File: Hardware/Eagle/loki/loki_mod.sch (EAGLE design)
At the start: 36 parts

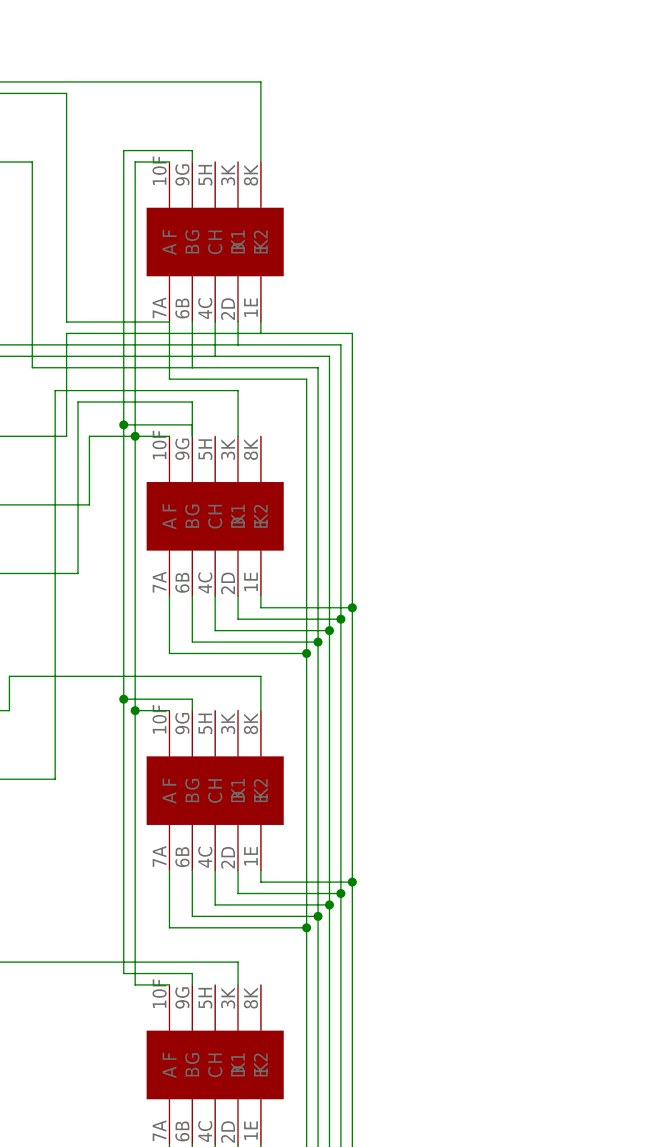
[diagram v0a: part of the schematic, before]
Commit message: Update the watch application to support the Loki module.
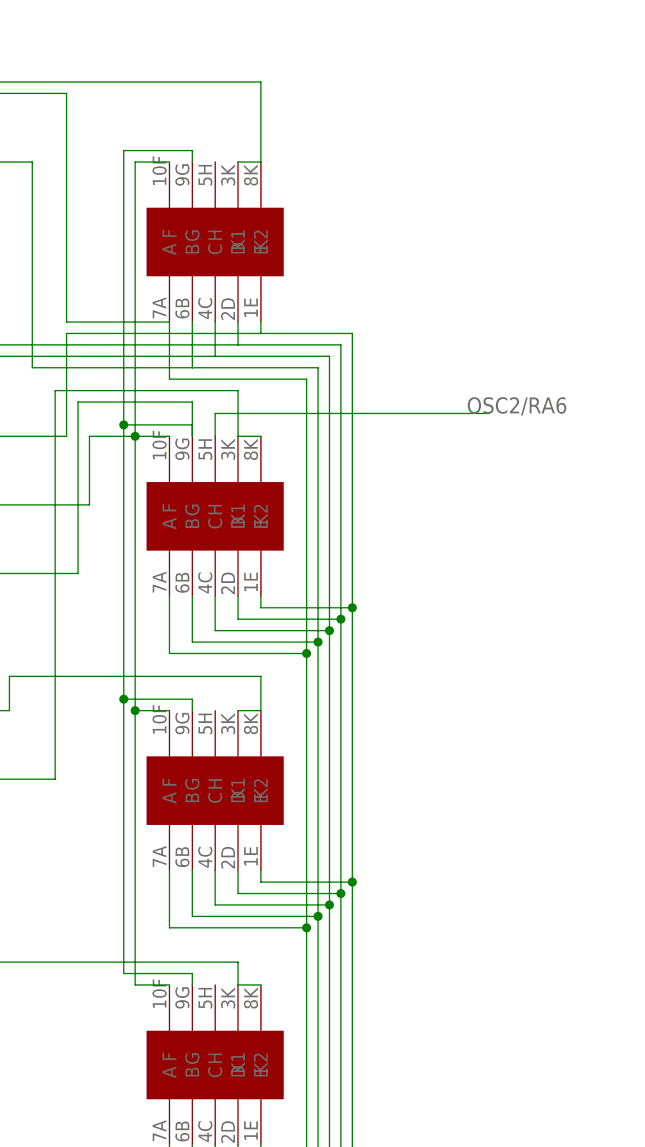
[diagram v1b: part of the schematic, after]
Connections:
- net OSC2/RA6: now also 1H.H
- net PGC/LED_M7: now also 10H.K1
- net RB1/LED_M6: now also 1H.K2
- net RB4/LED_H4: now also 10M.K1
- net RC3/LED_M4: now also 1M.K2
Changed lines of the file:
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@@
 <setting verticaltext="up"/>
 </settings>
-<grid distance="0.05" unitdist="inch" unit="inch" style="lines" multiple="1" display="no" altdistance="0.01" altunitdist="inch" altunit="inch"/>
+<grid distance="0.1" unitdist="inch" unit="inch" style="lines" multiple="1" display="no" altdistance="0.01" altunitdist="inch" altunit="inch"/>
 <layers>
 <layer number="1" name="Top" color="4" fill="1" visible="no" active="no"/>
@@
 <wire x1="-20.32" y1="-41.91" x2="7.62" y2="-41.91" width="0.1524" layer="91"/>
 <wire x1="7.62" y1="-41.91" x2="7.62" y2="-45.72" width="0.1524" layer="91"/>
+<pinref part="10M" gate="G$1" pin="K1"/>
+<wire x1="5.08" y1="-45.72" x2="7.62" y2="-45.72" width="0.1524" layer="91"/>
 </segment>
 </net>
@@
 <wire x1="-21.59" y1="-73.66" x2="5.08" y2="-73.66" width="0.1524" layer="91"/>
 <wire x1="5.08" y1="-73.66" x2="5.08" y2="-76.2" width="0.1524" layer="91"/>
+<pinref part="1M" gate="G$1" pin="K2"/>
+<wire x1="5.08" y1="-76.2" x2="7.62" y2="-76.2" width="0.1524" layer="91"/>
 </segment>
 </net>
@@
 <wire x1="-36.83" y1="24.13" x2="7.62" y2="24.13" width="0.1524" layer="91"/>
 <wire x1="7.62" y1="24.13" x2="7.62" y2="15.24" width="0.1524" layer="91"/>
+<pinref part="10H" gate="G$1" pin="K1"/>
+<wire x1="5.08" y1="15.24" x2="7.62" y2="15.24" width="0.1524" layer="91"/>
 </segment>
 <segment>
@@
 <wire x1="-15.24" y1="-10.16" x2="5.08" y2="-10.16" width="0.1524" layer="91"/>
 <wire x1="5.08" y1="-10.16" x2="5.08" y2="-15.24" width="0.1524" layer="91"/>
+<pinref part="1H" gate="G$1" pin="K2"/>
+<wire x1="5.08" y1="-15.24" x2="7.62" y2="-15.24" width="0.1524" layer="91"/>
 </segment>
 </net>
@@
 <label x="30.48" y="111.76" size="1.778" layer="95"/>
 </segment>
-</net>
+<segment>
+<pinref part="1H" gate="G$1" pin="H"/>
+<wire x1="2.54" y1="-15.24" x2="2.54" y2="-12.7" width="0.1524" layer="91"/>
+<wire x1="2.54" y1="-12.7" x2="33.02" y2="-12.7" width="0.1524" layer="91"/>
+<label x="30.48" y="-12.7" size="1.778" layer="95"/>
+</segment>
+</net>

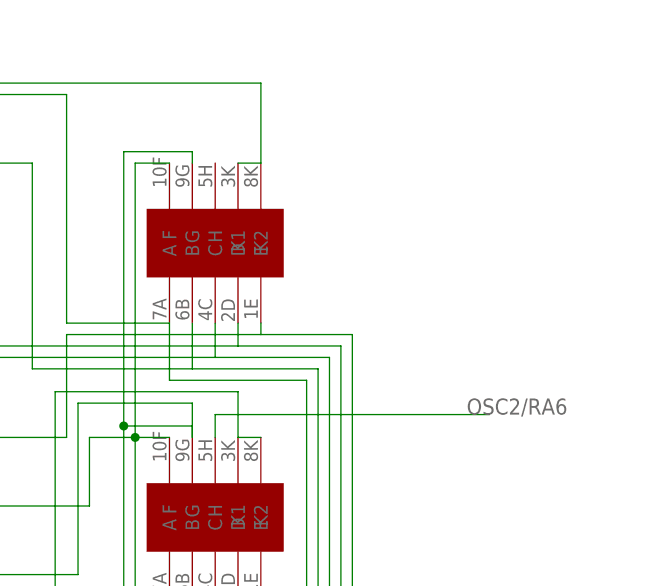
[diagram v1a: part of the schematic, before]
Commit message: Added resitor for date dot, if using the USSR replacement made display.
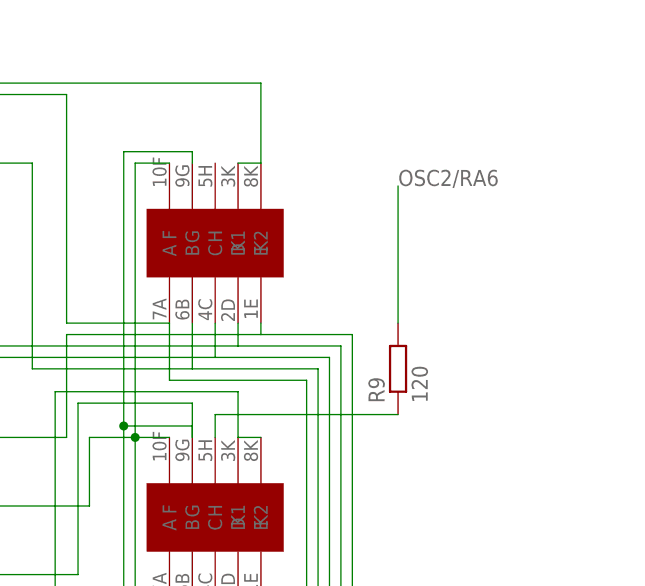
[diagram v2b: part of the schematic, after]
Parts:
- added R9: 120, resistor:R-EU_R0402
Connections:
- new net N$1: 1H.H, R9.1
- net OSC2/RA6: now also R9.2; no longer 1H.H
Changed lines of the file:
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@@
 <part name="10M" library="l104g" deviceset="L104G" device=""/>
 <part name="1M" library="l104g" deviceset="L104G" device=""/>
+<part name="R9" library="resistor" deviceset="R-EU_" device="R0402" value="120"/>
 </parts>
 <sheets>
@@
 <instance part="10M" gate="G$1" x="12.7" y="-33.02" rot="R90"/>
 <instance part="1M" gate="G$1" x="12.7" y="-63.5" rot="R90"/>
+<instance part="R9" gate="G$1" x="22.86" y="-7.62" rot="R90"/>
 </instances>
 <busses>
@@
 </segment>
 <segment>
-<pinref part="1H" gate="G$1" pin="H"/>
-<wire x1="2.54" y1="-15.24" x2="2.54" y2="-12.7" width="0.1524" layer="91"/>
-<wire x1="2.54" y1="-12.7" x2="33.02" y2="-12.7" width="0.1524" layer="91"/>
-<label x="30.48" y="-12.7" size="1.778" layer="95"/>
+<pinref part="R9" gate="G$1" pin="2"/>
+<wire x1="22.86" y1="-2.54" x2="22.86" y2="12.7" width="0.1524" layer="91"/>
+<label x="22.86" y="12.7" size="1.778" layer="95"/>
 </segment>
 </net>
@@
 </segment>
 </net>
+<net name="N$1" class="0">
+<segment>
+<pinref part="1H" gate="G$1" pin="H"/>
+<wire x1="2.54" y1="-15.24" x2="2.54" y2="-12.7" width="0.1524" layer="91"/>
+<wire x1="2.54" y1="-12.7" x2="22.86" y2="-12.7" width="0.1524" layer="91"/>
+<pinref part="R9" gate="G$1" pin="1"/>
+</segment>
+</net>

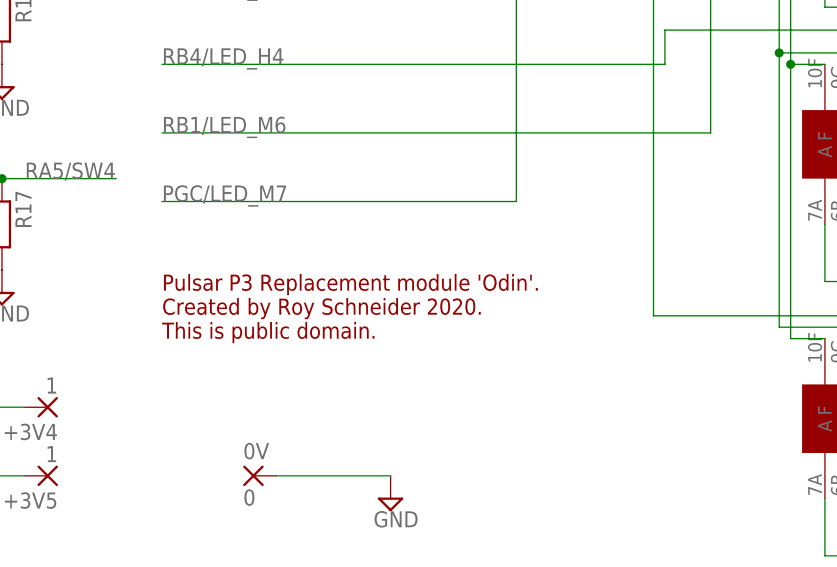
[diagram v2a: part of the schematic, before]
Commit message: Increased TRACE and VIA width were possible.
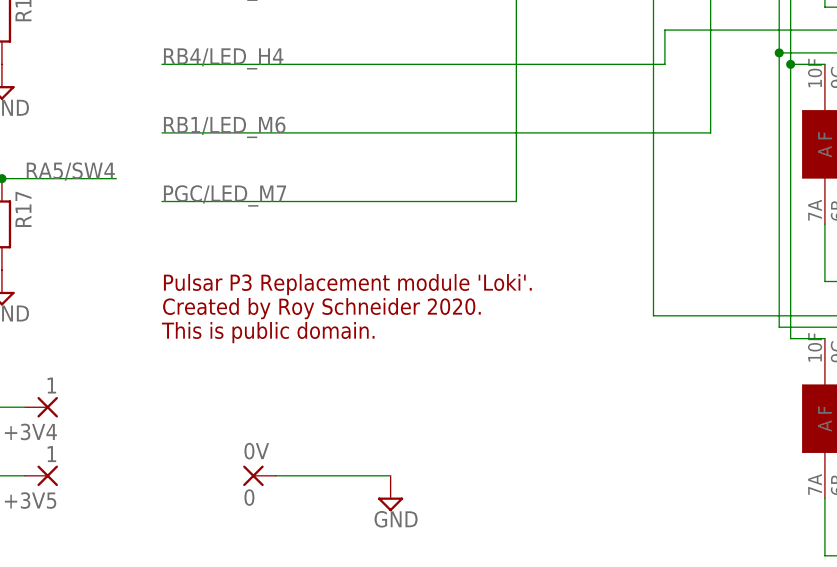
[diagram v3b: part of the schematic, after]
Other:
- note added: "Pulsar P3 Replacement module 'Loki'. Created by Roy Schneider 2020. This is public domain."
- note removed: "Pulsar P3 Replacement module 'Odin'. Created by Roy Schneider 2020. This is public domain."
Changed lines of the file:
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@@
 <text x="-120.904" y="143.002" size="1.778" layer="94">You might use a classical Xtal or a Low Power oscillator chip here.
 In the case of using an oscillator chip, connect its output to the OSI and leave OSO open.</text>
-<text x="-76.2" y="-76.2" size="1.778" layer="94">Pulsar P3 Replacement module 'Odin'.
+<text x="-76.2" y="-76.2" size="1.778" layer="94">Pulsar P3 Replacement module 'Loki'.
 Created by Roy Schneider 2020.
 This is public domain.</text>

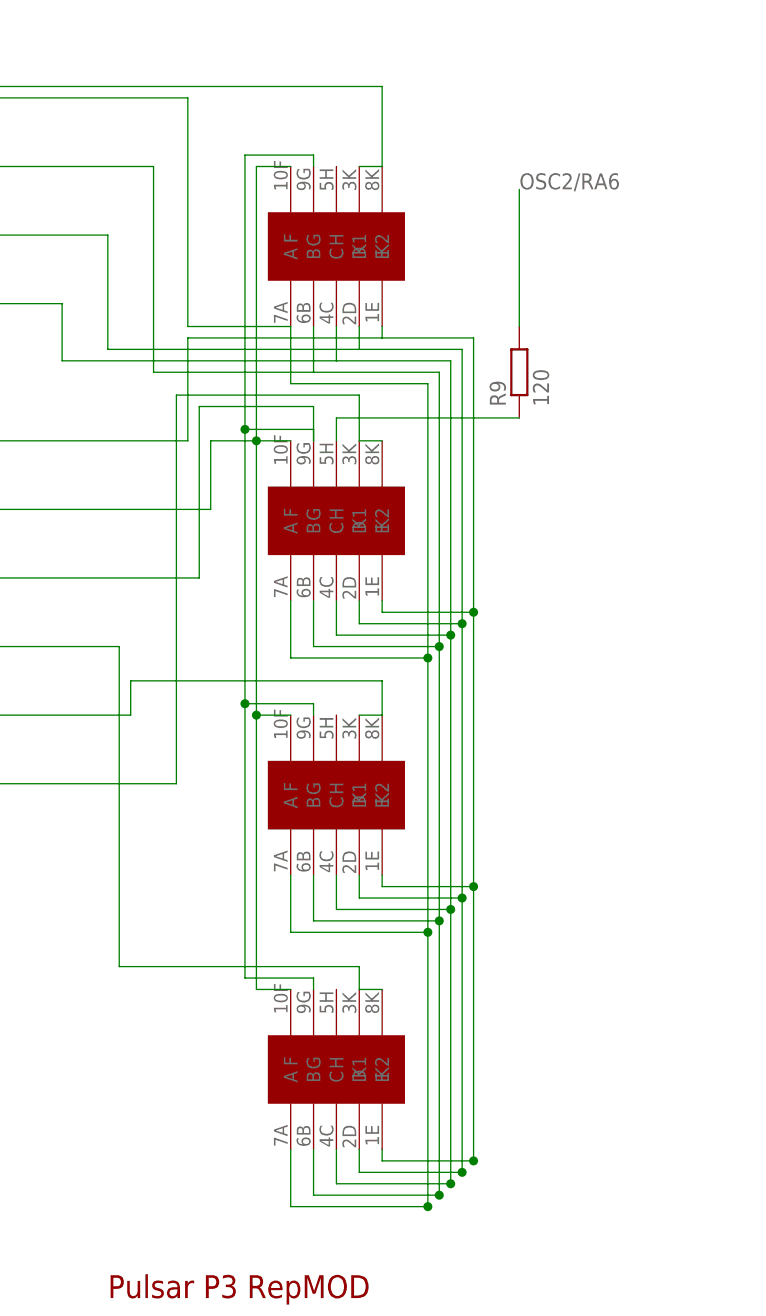
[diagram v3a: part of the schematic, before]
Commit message: Added alarm decimal point.
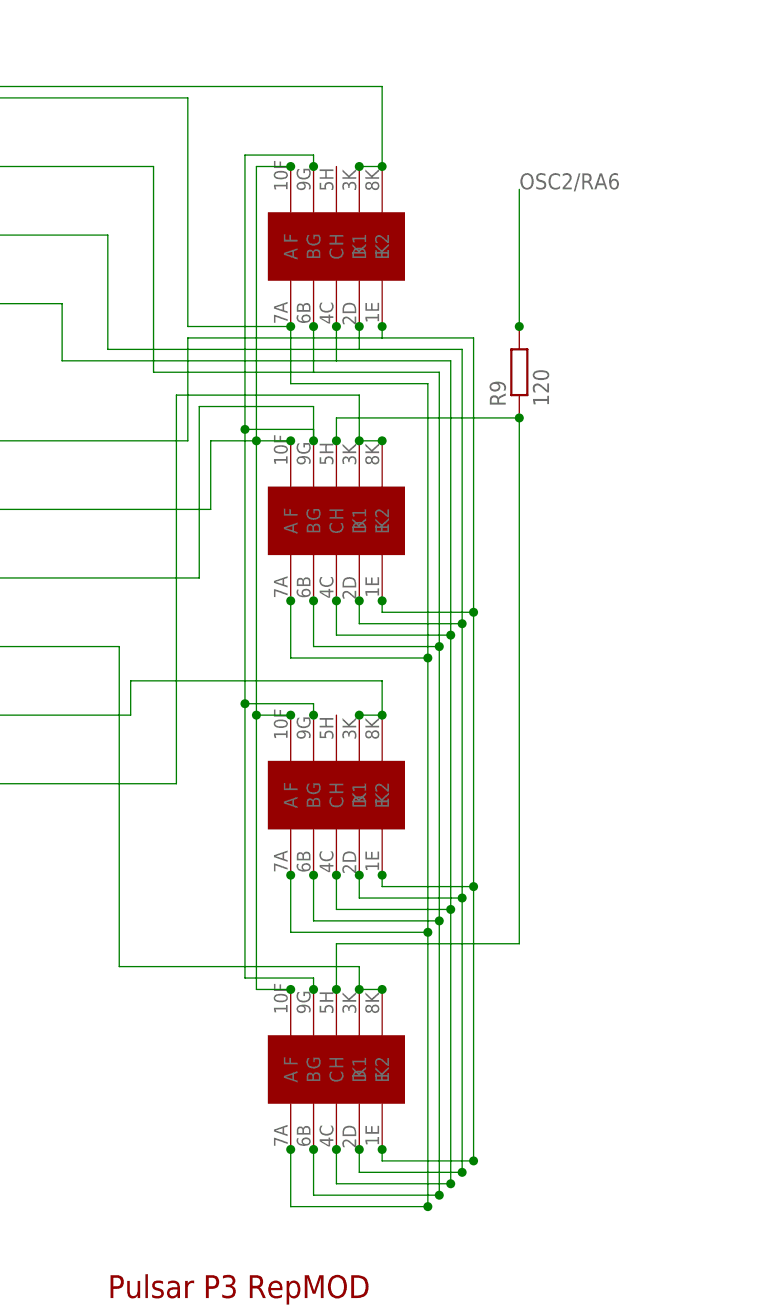
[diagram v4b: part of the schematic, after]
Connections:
- net N$1: now also 1M.H
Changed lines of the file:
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@@
 <pinref part="10M" gate="G$1" pin="K1"/>
 <wire x1="5.08" y1="-45.72" x2="7.62" y2="-45.72" width="0.1524" layer="91"/>
+<junction x="7.62" y="-45.72"/>
+<junction x="5.08" y="-45.72"/>
 </segment>
 </net>
@@
 <pinref part="1M" gate="G$1" pin="K2"/>
 <wire x1="5.08" y1="-76.2" x2="7.62" y2="-76.2" width="0.1524" layer="91"/>
+<junction x="7.62" y="-76.2"/>
+<junction x="5.08" y="-76.2"/>
 </segment>
 </net>
@@
 <pinref part="10H" gate="G$1" pin="K1"/>
 <wire x1="5.08" y1="15.24" x2="7.62" y2="15.24" width="0.1524" layer="91"/>
+<junction x="5.08" y="15.24"/>
+<junction x="7.62" y="15.24"/>
 </segment>
 <segment>
@@
 <pinref part="1H" gate="G$1" pin="K2"/>
 <wire x1="5.08" y1="-15.24" x2="7.62" y2="-15.24" width="0.1524" layer="91"/>
+<junction x="7.62" y="-15.24"/>
+<junction x="5.08" y="-15.24"/>
 </segment>
 </net>
@@
 <wire x1="22.86" y1="-2.54" x2="22.86" y2="12.7" width="0.1524" layer="91"/>
 <label x="22.86" y="12.7" size="1.778" layer="95"/>
+<junction x="22.86" y="-2.54"/>
 </segment>
 </net>
@@
 <pinref part="R7" gate="G$1" pin="2"/>
 <wire x1="-11.43" y1="-22.86" x2="-48.26" y2="-22.86" width="0.1524" layer="91"/>
+<junction x="-2.54" y="15.24"/>
+<junction x="-2.54" y="-15.24"/>
+<junction x="-2.54" y="-45.72"/>
+<junction x="-2.54" y="-76.2"/>
 </segment>
 </net>
@@
 <pinref part="R8" gate="G$1" pin="2"/>
 <wire x1="-12.7" y1="-30.48" x2="-48.26" y2="-30.48" width="0.1524" layer="91"/>
+<junction x="0" y="15.24"/>
+<junction x="0" y="-15.24"/>
+<junction x="0" y="-45.72"/>
+<junction x="0" y="-76.2"/>
 </segment>
 </net>
@@
 <pinref part="R2" gate="G$1" pin="2"/>
 <wire x1="-13.97" y1="22.86" x2="-48.26" y2="22.86" width="0.1524" layer="91"/>
+<junction x="-2.54" y="-2.54"/>
+<junction x="-2.54" y="-33.02"/>
+<junction x="-2.54" y="-63.5"/>
+<junction x="-2.54" y="-93.98"/>
 </segment>
 </net>
@@
 <pinref part="R3" gate="G$1" pin="2"/>
 <wire x1="-17.78" y1="15.24" x2="-48.26" y2="15.24" width="0.1524" layer="91"/>
+<junction x="0" y="-2.54"/>
+<junction x="0" y="-33.02"/>
+<junction x="0" y="-63.5"/>
+<junction x="0" y="-93.98"/>
 </segment>
 </net>
@@
 <pinref part="R5" gate="G$1" pin="2"/>
 <wire x1="-27.94" y1="0" x2="-48.26" y2="0" width="0.1524" layer="91"/>
+<junction x="2.54" y="-2.54"/>
+<junction x="2.54" y="-33.02"/>
+<junction x="2.54" y="-63.5"/>
+<junction x="2.54" y="-93.98"/>
 </segment>
 </net>
@@
 <pinref part="R4" gate="G$1" pin="2"/>
 <wire x1="-22.86" y1="7.62" x2="-48.26" y2="7.62" width="0.1524" layer="91"/>
+<junction x="5.08" y="-2.54"/>
+<junction x="5.08" y="-33.02"/>
+<junction x="5.08" y="-63.5"/>
+<junction x="5.08" y="-93.98"/>
 </segment>
 </net>
@@
 <pinref part="R6" gate="G$1" pin="2"/>
 <wire x1="-13.97" y1="-15.24" x2="-48.26" y2="-15.24" width="0.1524" layer="91"/>
+<junction x="7.62" y="-2.54"/>
+<junction x="7.62" y="-33.02"/>
+<junction x="7.62" y="-63.5"/>
+<junction x="7.62" y="-93.98"/>
 </segment>
 </net>
@@
 <wire x1="2.54" y1="-12.7" x2="22.86" y2="-12.7" width="0.1524" layer="91"/>
 <pinref part="R9" gate="G$1" pin="1"/>
-</segment>
-</net>
+<junction x="22.86" y="-12.7"/>
+<junction x="2.54" y="-15.24"/>
+<pinref part="1M" gate="G$1" pin="H"/>
+<wire x1="2.54" y1="-76.2" x2="2.54" y2="-71.12" width="0.1524" layer="91"/>
+<wire x1="2.54" y1="-71.12" x2="22.86" y2="-71.12" width="0.1524" layer="91"/>
+<wire x1="22.86" y1="-71.12" x2="22.86" y2="-12.7" width="0.1524" layer="91"/>
+<junction x="2.54" y="-76.2"/>
+</segment>
+</net>

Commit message: Improved layout of Loki board using USSR made replacement display.
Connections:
- new net PIEZO: U$1.RC2/AN11/CTPLS/RP13
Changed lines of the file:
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@@
+</segment>
+</net>
+<net name="PIEZO" class="0">
+<segment>
+<pinref part="U$1" gate="A" pin="RC2/AN11/CTPLS/RP13"/>
+<wire x1="27.94" y1="101.6" x2="48.26" y2="101.6" width="0.1524" layer="91"/>
+<wire x1="48.26" y1="101.6" x2="48.26" y2="73.66" width="0.1524" layer="91"/>
+<wire x1="48.26" y1="73.66" x2="27.94" y2="73.66" width="0.1524" layer="91"/>
+<label x="27.94" y="73.66" size="1.778" layer="95"/>
 </segment>
 </net>
